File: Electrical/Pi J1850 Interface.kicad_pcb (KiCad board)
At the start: 2 copper layers, 81.5 x 53.5 mm, 71 parts, among them J1 TO ACCESSORIES, J2 FROM RADIO, J4 LINE OUT, J5 LINE IN, P1 RASPBERRY PI, Q1 BC817, Q2 BC817, Q3 BC807, Q4 BC807, Q5 BC817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

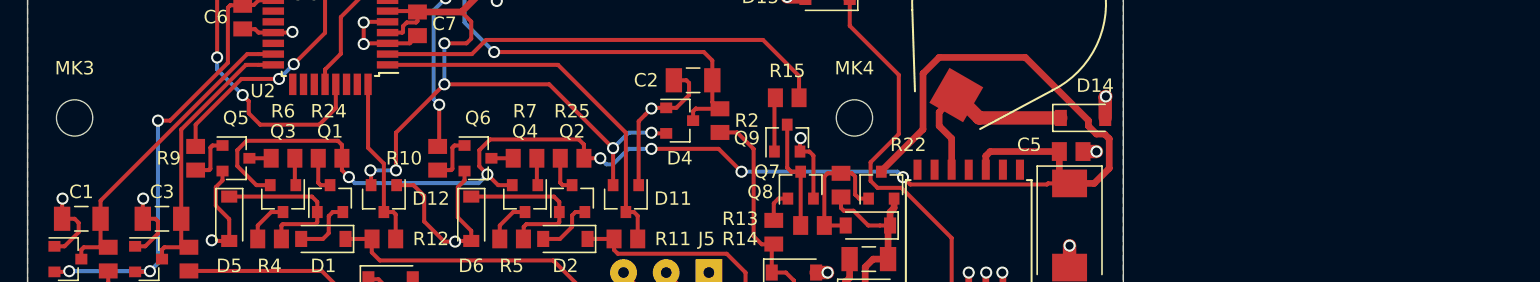
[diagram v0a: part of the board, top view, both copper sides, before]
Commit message: Updated schematic to reflect added pull downs for some transistors. Added mechanical model.
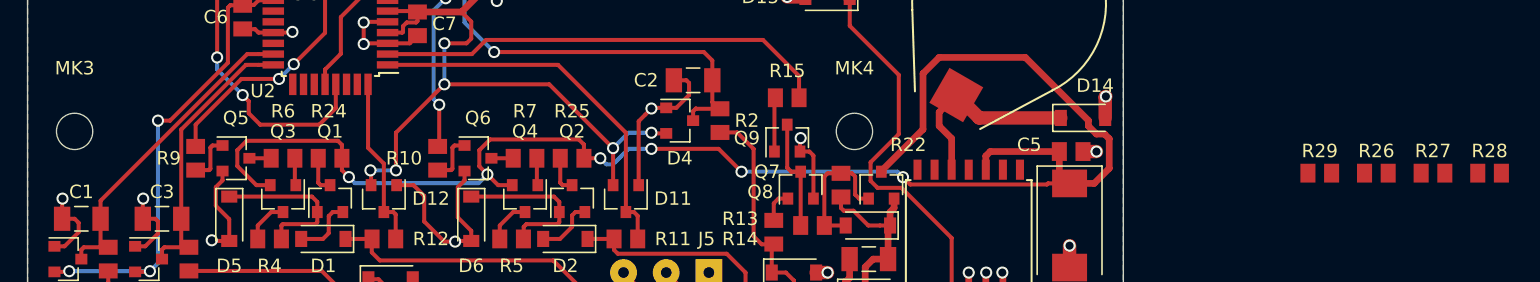
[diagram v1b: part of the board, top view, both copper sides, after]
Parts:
- added R26: 100k, Resistor_SMD:R_0805_2012Metric, F.Cu at (300.3, 123.6)
- added R27: 100k, Resistor_SMD:R_0805_2012Metric, F.Cu at (304.5, 123.6)
- added R28: 100k, Resistor_SMD:R_0805_2012Metric, F.Cu at (308.7, 123.6)
- added R29: 100k, Resistor_SMD:R_0805_2012Metric, F.Cu at (296.1, 123.6)
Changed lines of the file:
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@@
     (tracks 592)
     (zones 0)
-    (modules 71)
+    (modules 75)
     (nets 117)
   )
@@
   )
   (setup
-    (last_trace_width 1)
+    (last_trace_width 0.3)
     (user_trace_width 0.3)
     (user_trace_width 0.4)
@@
     (uvia_drill 0.1)
   )
+  (module Resistor_SMD:R_0805_2012Metric (layer F.Cu)
+    (at 308.738333 123.6075)
+    (descr "Resistor SMD 0805 (2012 Metric), square (rectangular) end terminal, IPC_7351 nominal, (Body size source: http://www.tortai-tech.com/upload/download/2011102023233369053.pdf), generated with kicad-footprint-generator")
+    (tags resistor)
+    (attr smd)
+    (fp_text reference R28 (at 0 -1.65) (layer F.SilkS)
+      (effects (font (size 1 1) (thickness 0.15)))
+    )
+    (fp_text value 100k (at 0 1.65) (layer F.Fab)
+      (effects (font (size 1 1) (thickness 0.15)))
+    )
+    (fp_text user %R (at 0 0) (layer F.Fab)
+      (effects (font (size 0.5 0.5) (thickness 0.08)))
+    )
+    (fp_line (start 1.69 0.95) (end -1.69 0.95) (layer F.CrtYd) (width 0.05))
+    (fp_line (start 1.69 -0.95) (end 1.69 0.95) (layer F.CrtYd) (width 0.05))
+    (fp_line (start -1.69 -0.95) (end 1.69 -0.95) (layer F.CrtYd) (width 0.05))
+    (fp_line (start -1.69 0.95) (end -1.69 -0.95) (layer F.CrtYd) (width 0.05))
+    (fp_line (start 1 0.6) (end -1 0.6) (layer F.Fab) (width 0.1))
+    (fp_line (start 1 -0.6) (end 1 0.6) (layer F.Fab) (width 0.1))
+    (fp_line (start -1 -0.6) (end 1 -0.6) (layer F.Fab) (width 0.1))
+    (fp_line (start -1 0.6) (end -1 -0.6) (layer F.Fab) (width 0.1))
+    (pad 2 smd rect (at 0.88 0) (size 1.12 1.4) (layers F.Cu F.Paste F.Mask)
+      (net 110 /J1850_IN_CMD_B))
+    (pad 1 smd rect (at -0.88 0) (size 1.12 1.4) (layers F.Cu F.Paste F.Mask)
+      (net 3 GND))
+    (model ${KISYS3DMOD}/Resistor_SMD.3dshapes/R_0805_2012Metric.wrl
+      (at (xyz 0 0 0))
+      (scale (xyz 1 1 1))
+      (rotate (xyz 0 0 0))
+    )
+  )
+  (module Resistor_SMD:R_0805_2012Metric (layer F.Cu)
+    (at 304.528333 123.6075)
+    (descr "Resistor SMD 0805 (2012 Metric), square (rectangular) end terminal, IPC_7351 nominal, (Body size source: http://www.tortai-tech.com/upload/download/2011102023233369053.pdf), generated with kicad-footprint-generator")
+    (tags resistor)
+    (attr smd)
+    (fp_text reference R27 (at 0 -1.65) (layer F.SilkS)
+      (effects (font (size 1 1) (thickness 0.15)))
+    )
+    (fp_text value 100k (at 0 1.65) (layer F.Fab)
+      (effects (font (size 1 1) (thickness 0.15)))
+    )
+    (fp_line (start -1 0.6) (end -1 -0.6) (layer F.Fab) (width 0.1))
+    (fp_line (start -1 -0.6) (end 1 -0.6) (layer F.Fab) (width 0.1))
+    (fp_line (start 1 -0.6) (end 1 0.6) (layer F.Fab) (width 0.1))
+    (fp_line (start 1 0.6) (end -1 0.6) (layer F.Fab) (width 0.1))
+    (fp_line (start -1.69 0.95) (end -1.69 -0.95) (layer F.CrtYd) (width 0.05))
+    (fp_line (start -1.69 -0.95) (end 1.69 -0.95) (layer F.CrtYd) (width 0.05))
+    (fp_line (start 1.69 -0.95) (end 1.69 0.95) (layer F.CrtYd) (width 0.05))
+    (fp_line (start 1.69 0.95) (end -1.69 0.95) (layer F.CrtYd) (width 0.05))
+    (fp_text user %R (at 0 0) (layer F.Fab)
+      (effects (font (size 0.5 0.5) (thickness 0.08)))
+    )
+    (pad 1 smd rect (at -0.88 0) (size 1.12 1.4) (layers F.Cu F.Paste F.Mask)
+      (net 3 GND))
+    (pad 2 smd rect (at 0.88 0) (size 1.12 1.4) (layers F.Cu F.Paste F.Mask)
+      (net 97 /PWR_HOLD_B))
+    (model ${KISYS3DMOD}/Resistor_SMD.3dshapes/R_0805_2012Metric.wrl
+      (at (xyz 0 0 0))
+      (scale (xyz 1 1 1))
+      (rotate (xyz 0 0 0))
+    )
+  )
+  (module Resistor_SMD:R_0805_2012Metric (layer F.Cu)
+    (at 300.318333 123.6075)
+    (descr "Resistor SMD 0805 (2012 Metric), square (rectangular) end terminal, IPC_7351 nominal, (Body size source: http://www.tortai-tech.com/upload/download/2011102023233369053.pdf), generated with kicad-footprint-generator")
+    (tags resistor)
+    (attr smd)
+    (fp_text reference R26 (at 0 -1.65) (layer F.SilkS)
+      (effects (font (size 1 1) (thickness 0.15)))
+    )
+    (fp_text value 100k (at 0 1.65) (layer F.Fab)
+      (effects (font (size 1 1) (thickness 0.15)))
+    )
+    (fp_text user %R (at 0 0) (layer F.Fab)
+      (effects (font (size 0.5 0.5) (thickness 0.08)))
+    )
+    (fp_line (start 1.69 0.95) (end -1.69 0.95) (layer F.CrtYd) (width 0.05))
+    (fp_line (start 1.69 -0.95) (end 1.69 0.95) (layer F.CrtYd) (width 0.05))
+    (fp_line (start -1.69 -0.95) (end 1.69 -0.95) (layer F.CrtYd) (width 0.05))
+    (fp_line (start -1.69 0.95) (end -1.69 -0.95) (layer F.CrtYd) (width 0.05))
+    (fp_line (start 1 0.6) (end -1 0.6) (layer F.Fab) (width 0.1))
+    (fp_line (start 1 -0.6) (end 1 0.6) (layer F.Fab) (width 0.1))
+    (fp_line (start -1 -0.6) (end 1 -0.6) (layer F.Fab) (width 0.1))
+    (fp_line (start -1 0.6) (end -1 -0.6) (layer F.Fab) (width 0.1))
+    (pad 2 smd rect (at 0.88 0) (size 1.12 1.4) (layers F.Cu F.Paste F.Mask)
+      (net 96 /ACC_B))
+    (pad 1 smd rect (at -0.88 0) (size 1.12 1.4) (layers F.Cu F.Paste F.Mask)
+      (net 3 GND))
+    (model ${KISYS3DMOD}/Resistor_SMD.3dshapes/R_0805_2012Metric.wrl
+      (at (xyz 0 0 0))
+      (scale (xyz 1 1 1))
+      (rotate (xyz 0 0 0))
+    )
+  )
+  (module Resistor_SMD:R_0805_2012Metric (layer F.Cu)
+    (at 296.108333 123.6075)
+    (descr "Resistor SMD 0805 (2012 Metric), square (rectangular) end terminal, IPC_7351 nominal, (Body size source: http://www.tortai-tech.com/upload/download/2011102023233369053.pdf), generated with kicad-footprint-generator")
+    (tags resistor)
+    (attr smd)
+    (fp_text reference R29 (at 0 -1.65) (layer F.SilkS)
+      (effects (font (size 1 1) (thickness 0.15)))
+    )
+    (fp_text value 100k (at 0 1.65) (layer F.Fab)
+      (effects (font (size 1 1) (thickness 0.15)))
+    )
+    (fp_line (start -1 0.6) (end -1 -0.6) (layer F.Fab) (width 0.1))
+    (fp_line (start -1 -0.6) (end 1 -0.6) (layer F.Fab) (width 0.1))
+    (fp_line (start 1 -0.6) (end 1 0.6) (layer F.Fab) (width 0.1))
+    (fp_line (start 1 0.6) (end -1 0.6) (layer F.Fab) (width 0.1))
+    (fp_line (start -1.69 0.95) (end -1.69 -0.95) (layer F.CrtYd) (width 0.05))
+    (fp_line (start -1.69 -0.95) (end 1.69 -0.95) (layer F.CrtYd) (width 0.05))
+    (fp_line (start 1.69 -0.95) (end 1.69 0.95) (layer F.CrtYd) (width 0.05))
+    (fp_line (start 1.69 0.95) (end -1.69 0.95) (layer F.CrtYd) (width 0.05))
+    (fp_text user %R (at 0 0) (layer F.Fab)
+      (effects (font (size 0.5 0.5) (thickness 0.08)))
+    )
+    (pad 1 smd rect (at -0.88 0) (size 1.12 1.4) (layers F.Cu F.Paste F.Mask)
+      (net 3 GND))
+    (pad 2 smd rect (at 0.88 0) (size 1.12 1.4) (layers F.Cu F.Paste F.Mask)
+      (net 109 /J1850_OUT_CMD_B))
+    (model ${KISYS3DMOD}/Resistor_SMD.3dshapes/R_0805_2012Metric.wrl
+      (at (xyz 0 0 0))
+      (scale (xyz 1 1 1))
+      (rotate (xyz 0 0 0))
+    )
+  )
   (module Connector_TE-Connectivity:TE_MULTI-LOCK_ProprietaryChryslerRadio_2x5_and_2x11_P2.5mm_and_P3mm_and_P3.5mm_Horizontal (layer F.Cu)
     (at 251 134.5)
@@
     (fp_circle (center 0 0) (end 2.7 0) (layer Cmts.User) (width 0.15))
     (fp_circle (center 0 0) (end 2.95 0) (layer F.CrtYd) (width 0.05))
-    (pad 1 np_thru_hole circle (at 0 0) (size 2.7 2.7) (drill 2.7) (layers *.Cu *.Mask))
+    (pad "" np_thru_hole circle (at 0 1) (size 2.7 2.7) (drill 2.7) (layers *.Cu *.Mask))
   )
   (module MountingHole:MountingHole_2.7mm_M2.5 (layer F.Cu)
@@
     (fp_circle (center 0 0) (end 2.7 0) (layer Cmts.User) (width 0.15))
     (fp_circle (center 0 0) (end 2.95 0) (layer F.CrtYd) (width 0.05))
-    (pad 1 np_thru_hole circle (at 0 0) (size 2.7 2.7) (drill 2.7) (layers *.Cu *.Mask))
+    (pad "" np_thru_hole circle (at 0 1) (size 2.7 2.7) (drill 2.7) (layers *.Cu *.Mask))
   )
   (module MountingHole:MountingHole_2.7mm_M2.5 (layer F.Cu)
